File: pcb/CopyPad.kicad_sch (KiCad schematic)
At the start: 9 parts, among them J1 OLED_128x32, SW1 SW_Push, SW2 SW_Push, SW3 SW_Push, SW4 RotaryEncoder_Switch, U1 XIAO-RP2040-DIP

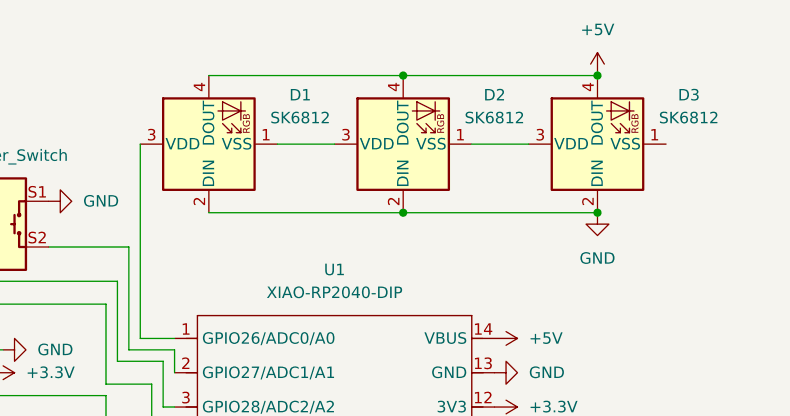
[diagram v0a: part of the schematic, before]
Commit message: update to replace SK6812 with SK6812 MINI
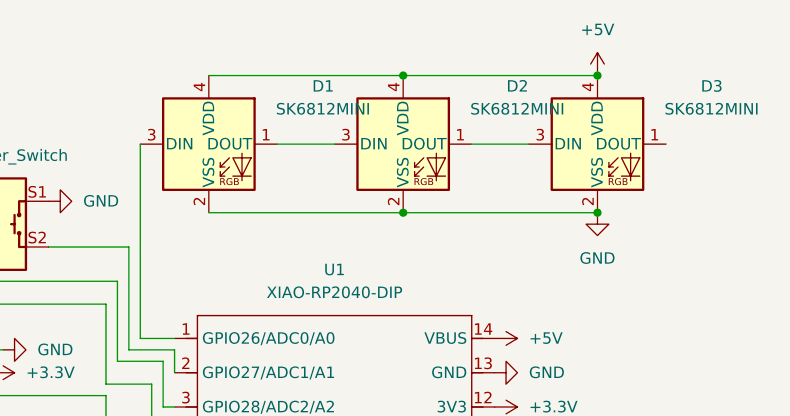
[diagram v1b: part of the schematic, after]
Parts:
- removed D1, D2, D3: SK6812, LED_SMD:LED_SK6812_PLCC4_5.0x5.0mm_P3.2mm, symbol LED:SK6812
- added D1, D2, D3: SK6812MINI, LED_SMD:LED_SK6812MINI_PLCC4_3.5x3.5mm_P1.75mm, symbol LED:SK6812MINI
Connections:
- net +5V: now also D1.4 (VDD), D2.4 (VDD), D3.4 (VDD)
- net GND: now also D1.2 (VSS), D2.2 (VSS), D3.2 (VSS)
- net at U1.1 (GPIO26/ADC0/A0): now also D1.3 (DIN)
- new net: D2.1 (DOUT), D3.3 (DIN)
- new net: D1.1 (DOUT), D2.3 (DIN)
